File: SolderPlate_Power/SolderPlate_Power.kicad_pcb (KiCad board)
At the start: 2 copper layers, 102 x 21 mm, 22 parts, among them J1 N, J2 Fan, J3 L, J4 SSR, J5 LCD, J7 uCont, Q1 BSS138, Q2 BSS138, Q3 BSS138

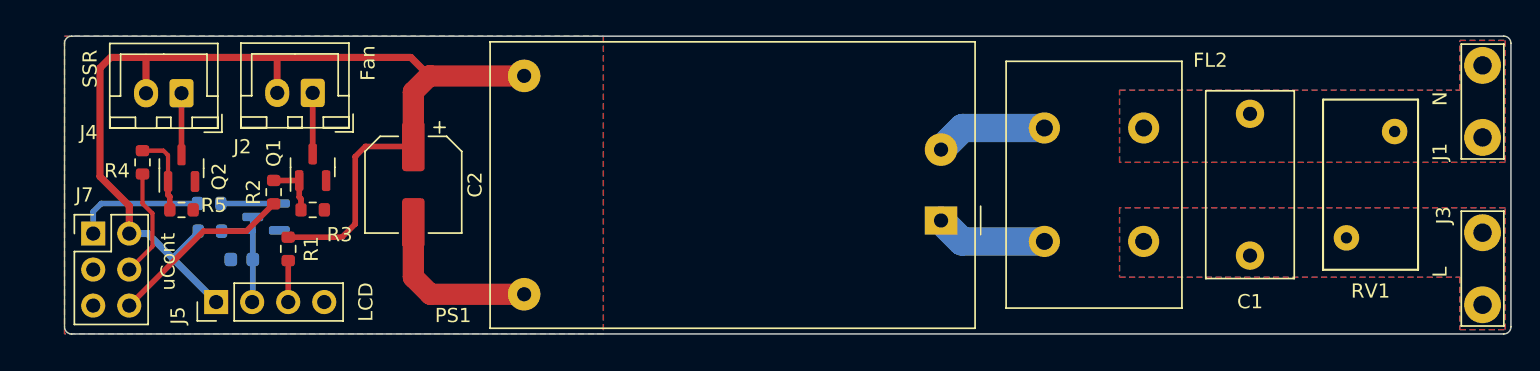
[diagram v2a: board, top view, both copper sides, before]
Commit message: Final PCBs and production files. Added latch for control wheel circuit
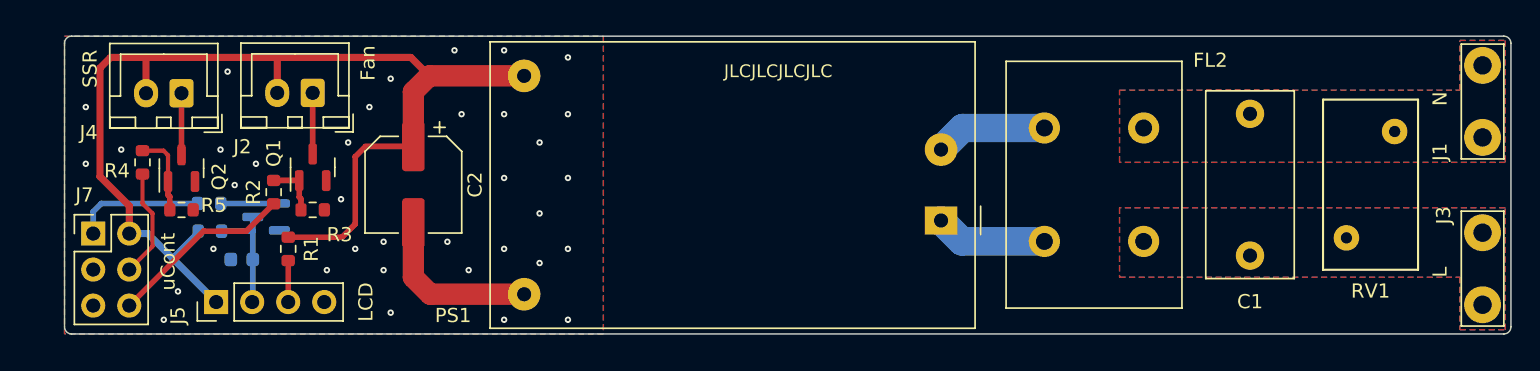
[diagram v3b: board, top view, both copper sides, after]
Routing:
- net GND: vias 0 -> 36
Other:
- board text added: "JLCJLCJLCJLC"
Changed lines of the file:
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@@
     )
     (pad_to_mask_clearance 0)
-    (aux_axis_origin 86.5 73)
+    (aux_axis_origin 89 73)
     (pcbplotparams
       (layerselection 0x00010fc_ffffffff)
@@
     (fp_line (start 4.95 3.4) (end 4.95 -2.35)
       (stroke (width 0.1) (type solid)) (layer "F.Fab"))
-    (pad "1" thru_hole roundrect (at 0 0 180) (size 1.7 2) (drill 1) (layers "*.Cu" "*.Mask") (roundrect_rratio 0.147059)
+    (pad "1" thru_hole roundrect (at 0 0 180) (size 1.7 2) (drill 1) (layers "*.Cu" "*.Mask") (roundrect_rratio 0.1470588235)
       (net 11 "Net-(J4-Pin_1)") (pinfunction "Pin_1") (pintype "passive"))
     (pad "2" thru_hole oval (at 2.5 0 180) (size 1.7 2) (drill 1) (layers "*.Cu" "*.Mask")
@@
     (fp_line (start 4.95 3.4) (end 4.95 -2.35)
       (stroke (width 0.1) (type solid)) (layer "F.Fab"))
-    (pad "1" thru_hole roundrect (at 0 0 180) (size 1.7 2) (drill 1) (layers "*.Cu" "*.Mask") (roundrect_rratio 0.147059)
+    (pad "1" thru_hole roundrect (at 0 0 180) (size 1.7 2) (drill 1) (layers "*.Cu" "*.Mask") (roundrect_rratio 0.1470588235)
       (net 9 "Net-(J2-Pin_1)") (pinfunction "Pin_1") (pintype "passive"))
     (pad "2" thru_hole oval (at 2.5 0 180) (size 1.7 2) (drill 1) (layers "*.Cu" "*.Mask")
@@
   (gr_line (start 89.5 52) (end 190.5 52)
     (stroke (width 0.1) (type default)) (layer "Edge.Cuts"))
+  (gr_text "JLCJLCJLCJLC" (at 135.5 55) (layer "F.SilkS")
+    (effects (font (size 0.9 0.9) (thickness 0.15)) (justify left bottom))
+  )
   (dimension (type aligned) (layer "Cmts.User")
     (pts (xy 191 74) (xy 89 74))
@@
   (segment (start 121.4125 70.2) (end 114.8 70.2) (width 1.5) (layer "F.Cu") (net 3))
   (segment (start 114.8 70.2) (end 113.6 69) (width 1.5) (layer "F.Cu") (net 3))
+  (via (at 122.5 64.5) (size 0.45) (drill 0.2) (layers "F.Cu" "B.Cu") (free) (net 3))
+  (via (at 120 72) (size 0.45) (drill 0.2) (layers "F.Cu" "B.Cu") (free) (net 3))
+  (via (at 124.5 53.5) (size 0.45) (drill 0.2) (layers "F.Cu" "B.Cu") (free) (net 3))
+  (via (at 112 55) (size 0.45) (drill 0.2) (layers "F.Cu" "B.Cu") (free) (net 3))
+  (via (at 111.5 68.5) (size 0.45) (drill 0.2) (layers "F.Cu" "B.Cu") (free) (net 3))
+  (via (at 124.5 57.5) (size 0.45) (drill 0.2) (layers "F.Cu" "B.Cu") (free) (net 3))
+  (via (at 120 62) (size 0.45) (drill 0.2) (layers "F.Cu" "B.Cu") (free) (net 3))
+  (via (at 90.5 61) (size 0.45) (drill 0.2) (layers "F.Cu" "B.Cu") (free) (net 3))
+  (via (at 120 53) (size 0.45) (drill 0.2) (layers "F.Cu" "B.Cu") (free) (net 3))
+  (via (at 124.5 72) (size 0.45) (drill 0.2) (layers "F.Cu" "B.Cu") (free) (net 3))
+  (via (at 100 60) (size 0.45) (drill 0.2) (layers "F.Cu" "B.Cu") (free) (net 3))
+  (via (at 110.5 57) (size 0.45) (drill 0.2) (layers "F.Cu" "B.Cu") (free) (net 3))
+  (via (at 116 66.5) (size 0.45) (drill 0.2) (layers "F.Cu" "B.Cu") (free) (net 3))
+  (via (at 124.5 67) (size 0.45) (drill 0.2) (layers "F.Cu" "B.Cu") (free) (net 3))
+  (via (at 101 62.5) (size 0.45) (drill 0.2) (layers "F.Cu" "B.Cu") (free) (net 3))
+  (via (at 109.5 67) (size 0.45) (drill 0.2) (layers "F.Cu" "B.Cu") (free) (net 3))
+  (via (at 120 57.5) (size 0.45) (drill 0.2) (layers "F.Cu" "B.Cu") (free) (net 3))
+  (via (at 117.5 68.5) (size 0.45) (drill 0.2) (layers "F.Cu" "B.Cu") (free) (net 3))
+  (via (at 117 57.5) (size 0.45) (drill 0.2) (layers "F.Cu" "B.Cu") (free) (net 3))
+  (via (at 107.5 68.5) (size 0.45) (drill 0.2) (layers "F.Cu" "B.Cu") (free) (net 3))
+  (via (at 112 71.5) (size 0.45) (drill 0.2) (layers "F.Cu" "B.Cu") (free) (net 3))
+  (via (at 97 70) (size 0.45) (drill 0.2) (layers "F.Cu" "B.Cu") (free) (net 3))
+  (via (at 99.5 67) (size 0.45) (drill 0.2) (layers "F.Cu" "B.Cu") (free) (net 3))
+  (via (at 96 72) (size 0.45) (drill 0.2) (layers "F.Cu" "B.Cu") (free) (net 3))
+  (via (at 109 59.5) (size 0.45) (drill 0.2) (layers "F.Cu" "B.Cu") (free) (net 3))
+  (via (at 116.5 53) (size 0.45) (drill 0.2) (layers "F.Cu" "B.Cu") (free) (net 3))
+  (via (at 124.5 62) (size 0.45) (drill 0.2) (layers "F.Cu" "B.Cu") (free) (net 3))
+  (via (at 90.5 57) (size 0.45) (drill 0.2) (layers "F.Cu" "B.Cu") (free) (net 3))
+  (via (at 111.5 66.5) (size 0.45) (drill 0.2) (layers "F.Cu" "B.Cu") (free) (net 3))
+  (via (at 108.5 63.5) (size 0.45) (drill 0.2) (layers "F.Cu" "B.Cu") (free) (net 3))
+  (via (at 122.5 59.5) (size 0.45) (drill 0.2) (layers "F.Cu" "B.Cu") (free) (net 3))
+  (via (at 120 67) (size 0.45) (drill 0.2) (layers "F.Cu" "B.Cu") (free) (net 3))
+  (via (at 100.5 54.5) (size 0.45) (drill 0.2) (layers "F.Cu" "B.Cu") (free) (net 3))
+  (via (at 93 60) (size 0.45) (drill 0.2) (layers "F.Cu" "B.Cu") (free) (net 3))
+  (via (at 102.5 61) (size 0.45) (drill 0.2) (layers "F.Cu" "B.Cu") (free) (net 3))
+  (via (at 122.5 68) (size 0.45) (drill 0.2) (layers "F.Cu" "B.Cu") (free) (net 3))
   (segment (start 158.1 66.475) (end 152.2875 66.475) (width 2) (layer "B.Cu") (net 4))
   (segment (start 152.2875 66.475) (end 150.8125 65) (width 2) (layer "B.Cu") (net 4))
